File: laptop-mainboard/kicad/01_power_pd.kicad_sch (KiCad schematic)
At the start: 30 parts, among them Q1 SiSS22DN, Q2 SiSS22DN, Q3 SiSS22DN, Q4 SiSS22DN, Q5 SiSS22DN, U1 TPS65988DH, U18 TPS62823, U2 W25Q80DV_PDCFG, U3 BQ25731, U4 MPQ8633B, U5 MPQ8633B, U6 TPS62823, U7 TPS62823, U8 TPS62823, U9 MPQ8633B

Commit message: Rev B: echte AM5-Pinbelegung, Kleinteile, EliteBook-850-G7-Format
- AM5-Pinmap (1718 Pins, WikiChip/Wikimedia Public Domain) als CSV,
  Sockel-Footprint mit echten Padnamen und 1708 Signal-Netzen im Board
- Blatt 10: MLCC-Baenke, 11 ESD-Arrays, USB2-Chokes, Straps; 48-MHz-Quarz;
  beidseitige Bestueckung (B.Cu) mit Kollisionspruefung pro Seite
- Board 340x112mm im EliteBook-850-G7-Layout: USB-C-100W-PD an der
  Barrel-Jack-Position, TB4/HDMI/USB-A/RJ45 rechts, USB-A/Klinke links,
  HP-Akku 3S/56Wh, HP-FPC-Steckplaetze (Pinouts zu verifizieren)
- GND-Stitching-Vias, MDI-/DP-Korridore, 645 Board-Netze
- Renderer tools/render_board.py erzeugt docs/board_render.png
- Doku: elitebook.md neu, grenzen.md/README/power/layout aktualisiert

Co-Authored-By: Claude Fable 5 <noreply@anthropic.com>
Claude-Session: https://claude.ai/code/session_01E8mU1RUAv938Hs69waADCc
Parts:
- J_BAT: value AkkuStecker_4S -> AkkuStecker_HP_3S; symbol lm:AkkuStecker_4S_J_BAT -> lm:AkkuStecker_HP_3S_J_BAT
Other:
- note added: "-> TPS65988 Pfad-FET -> BQ25731. NVDC: +VSYS = max(Akku, Wandler)."
- note added: "Akku: HP-Original 3S Li-Ion 11.55V / 56Wh (EliteBook 850 G7)."
- note added: "Alle Bucks: Feedback-Teiler und MLCC-Entkopplung auf Blatt 10."
- note added: "Laden: 100W USB-PD (20V/5A) am Port TB0 (Position des HP-Barrel-Jacks)"
- note added: "Q5/R1: BATFET + Lade-Shunt; R2: Eingangsstrom-Shunt (ACP/ACN)."
- note removed: "Alle Bucks: Feedback-Teiler und MLCC-Entkopplung siehe docs/power.md."
- note removed: "Laden: 100W USB-PD (20V/5A) am Port TB0 -> TPS65988 Pfad-FET -> BQ25731."
- note removed: "NVDC-Topologie: +VSYS = max(Akku, Wandler); Akku 4S Li-Ion 15.4V / 80Wh."
- note removed: "R1-Hinweis: SW2-Knoten -> Shunt -> SRP/SRN -> BAT (Ladestrommessung)."
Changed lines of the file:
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@@
     (company "Laptop-Mainboard-Projekt")
   )
-  (text "Laden: 100W USB-PD (20V/5A) am Port TB0 -> TPS65988 Pfad-FET -> BQ25731." (exclude_from_sim no) (at 20 260 0)
-    (effects (font (size 1.6 1.6)) (justify left))
-  )
-  (text "NVDC-Topologie: +VSYS = max(Akku, Wandler); Akku 4S Li-Ion 15.4V / 80Wh." (exclude_from_sim no) (at 20 265 0)
-    (effects (font (size 1.6 1.6)) (justify left))
-  )
-  (text "R1-Hinweis: SW2-Knoten -> Shunt -> SRP/SRN -> BAT (Ladestrommessung)." (exclude_from_sim no) (at 20 270 0)
-    (effects (font (size 1.6 1.6)) (justify left))
-  )
-  (text "Alle Bucks: Feedback-Teiler und MLCC-Entkopplung siehe docs/power.md." (exclude_from_sim no) (at 20 275 0)
-    (effects (font (size 1.6 1.6)) (justify left))
-  )
-  (text "+3V3_ALW versorgt EC und PD-Controller auch im Soft-Off (S5)." (exclude_from_sim no) (at 20 280 0)
+  (text "Laden: 100W USB-PD (20V/5A) am Port TB0 (Position des HP-Barrel-Jacks)" (exclude_from_sim no) (at 20 260 0)
+    (effects (font (size 1.6 1.6)) (justify left))
+  )
+  (text "-> TPS65988 Pfad-FET -> BQ25731. NVDC: +VSYS = max(Akku, Wandler)." (exclude_from_sim no) (at 20 265 0)
+    (effects (font (size 1.6 1.6)) (justify left))
+  )
+  (text "Akku: HP-Original 3S Li-Ion 11.55V / 56Wh (EliteBook 850 G7)." (exclude_from_sim no) (at 20 270 0)
+    (effects (font (size 1.6 1.6)) (justify left))
+  )
+  (text "Q5/R1: BATFET + Lade-Shunt; R2: Eingangsstrom-Shunt (ACP/ACN)." (exclude_from_sim no) (at 20 275 0)
+    (effects (font (size 1.6 1.6)) (justify left))
+  )
+  (text "Alle Bucks: Feedback-Teiler und MLCC-Entkopplung auf Blatt 10." (exclude_from_sim no) (at 20 280 0)
+    (effects (font (size 1.6 1.6)) (justify left))
+  )
+  (text "+3V3_ALW versorgt EC und PD-Controller auch im Soft-Off (S5)." (exclude_from_sim no) (at 20 285 0)
     (effects (font (size 1.6 1.6)) (justify left))
   )
@@
     (property "Intersheetrefs" "${INTERSHEET_REFS}" (at 109.13 97.79 0) (effects (font (size 1.27 1.27)) (hide yes)))
   )
-  (symbol (lib_id "lm:AkkuStecker_4S_J_BAT") (at 85 124.46 0) (unit 1)
+  (symbol (lib_id "lm:AkkuStecker_HP_3S_J_BAT") (at 85 124.46 0) (unit 1)
     (exclude_from_sim no) (in_bom yes) (on_board yes) (dnp no)
     (property "Reference" "J_BAT" (at 85 109.22 0) (effects (font (size 1.27 1.27))))
-    (property "Value" "AkkuStecker_4S" (at 85 139.7 0) (effects (font (size 1.27 1.27))))
+    (property "Value" "AkkuStecker_HP_3S" (at 85 139.7 0) (effects (font (size 1.27 1.27))))
     (property "Footprint" "laptop_mainboard:CONN_BAT8_2mm" (at 85 124.46 0) (effects (font (size 1.27 1.27)) (hide yes)))
     (property "Datasheet" "" (at 85 124.46 0) (effects (font (size 1.27 1.27)) (hide yes)))

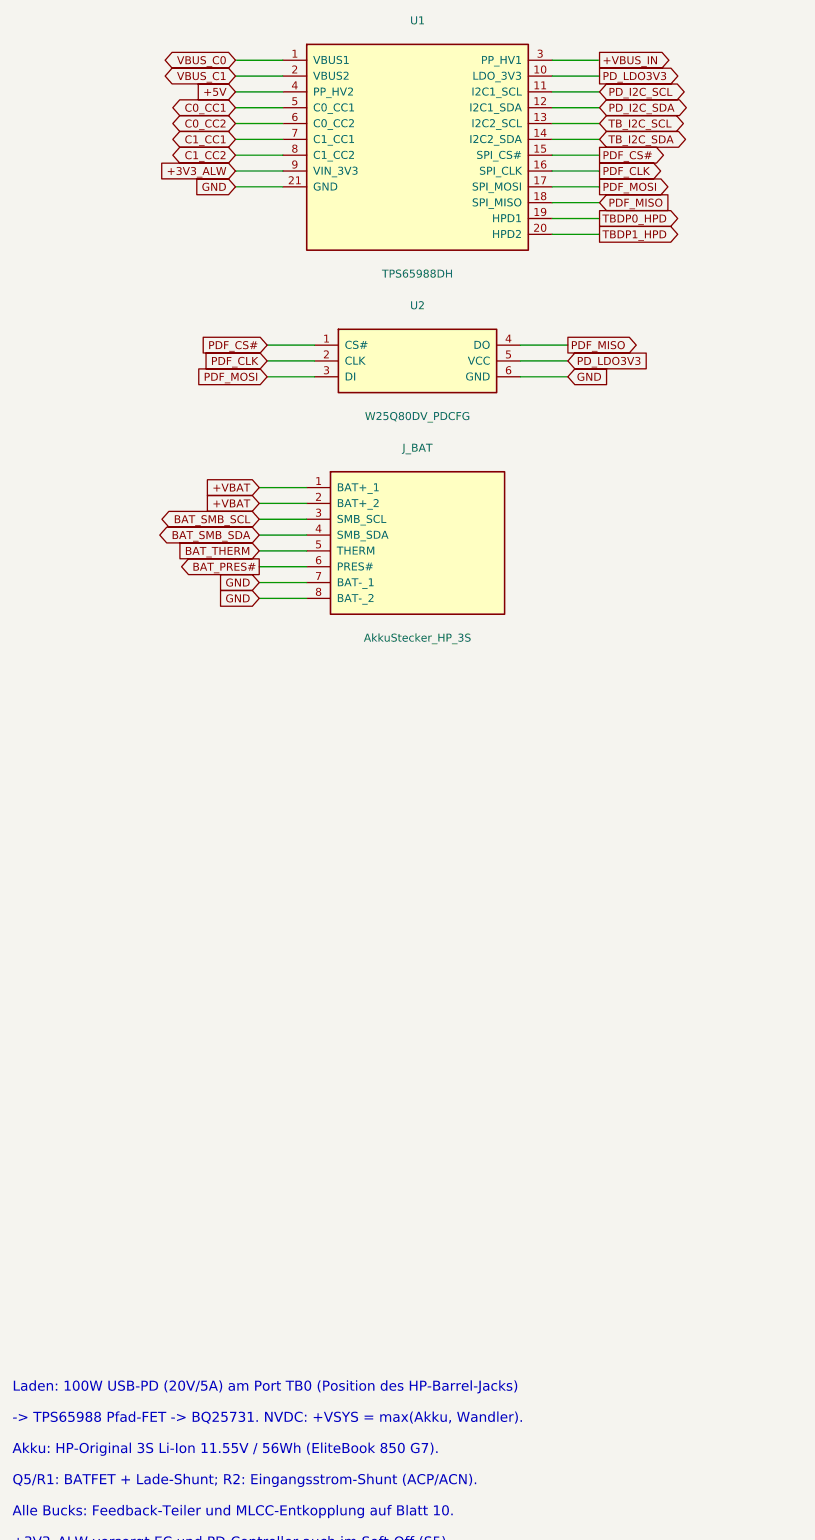
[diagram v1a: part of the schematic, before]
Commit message: Portlayout nach Fotos des Originalgeraets korrigiert
- Rechte Kante hinten->vorn: USB-C-Ladeport 100W (Barrel-Position,
  eigener TPS65987D + Config-Flash, neues Blatt 07_ladeport), USB-A,
  HDMI, 2x USB-C Thunderbolt 4 nebeneinander (JHL8540)
- Kein RJ45 (Original hat keines): Ethernet entfernt, G0/G1 Reserve
- TPS65988 nur noch Source fuer die TB-Ports; breite VBUS_IN-Trasse
  vom Ladeport zum BQ25731
- Interne Anschlusspositionen des Original-Mainboards (Nutzerfoto)
  als Referenztabelle in docs/elitebook.md dokumentiert
- Doku, Blockdiagramm, BOM und Rendering aktualisiert

Co-Authored-By: Claude Fable 5 <noreply@anthropic.com>
Claude-Session: https://claude.ai/code/session_01E8mU1RUAv938Hs69waADCc
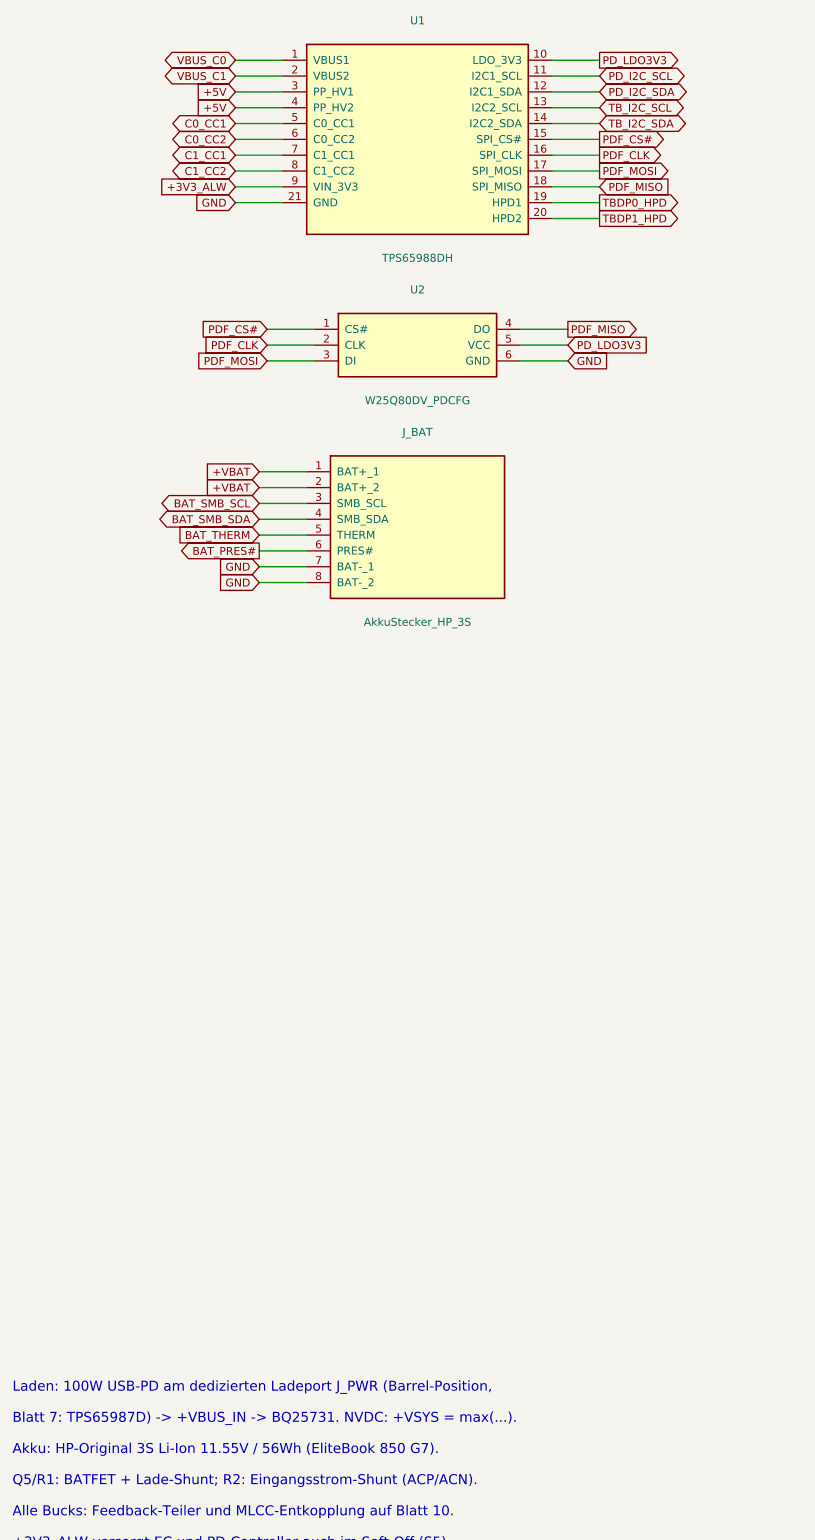
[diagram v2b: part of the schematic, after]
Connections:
- net +5V: now also U1.3 (PP_HV1)
- net +VBUS_IN: no longer U1.3 (PP_HV1)
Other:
- note added: "Blatt 7: TPS65987D) -> +VBUS_IN -> BQ25731. NVDC: +VSYS = max(...)."
- note added: "Laden: 100W USB-PD am dedizierten Ladeport J_PWR (Barrel-Position,"
- note removed: "-> TPS65988 Pfad-FET -> BQ25731. NVDC: +VSYS = max(Akku, Wandler)."
- note removed: "Laden: 100W USB-PD (20V/5A) am Port TB0 (Position des HP-Barrel-Jacks)"
- moved on the sheet: J_BAT, U1, U2
